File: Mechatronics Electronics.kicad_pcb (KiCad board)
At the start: 2 copper layers, 30.5 x 30 mm, 2 parts

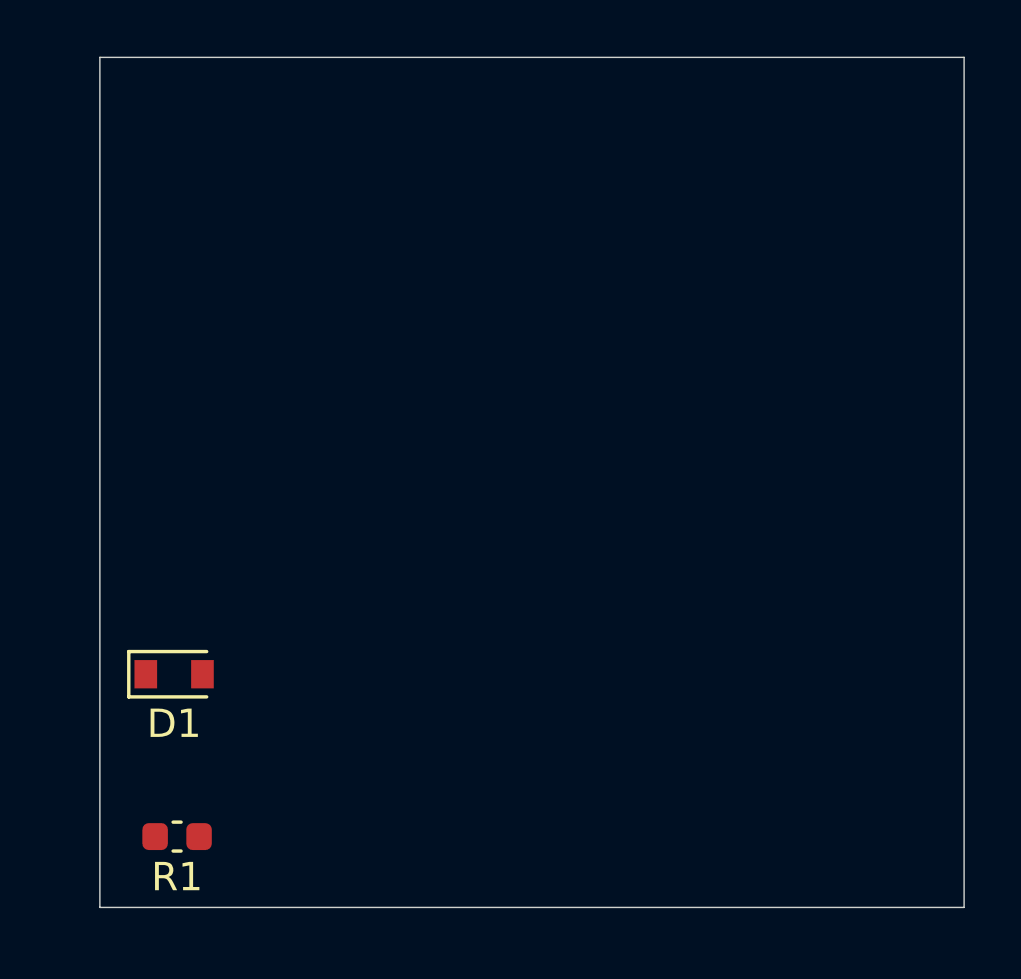
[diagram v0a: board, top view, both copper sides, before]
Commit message: Added TCAN4551-Q1 custom footprint/symbol and applied BGA microvia DRC rule
- Created and linked custom symbol + footprint for TCAN4551-Q1
- Added KiCad default MCIMX6D4AVT symbol
- Defined BGA_Area rule with microvia geometry:
  * Min annular width: 2 mil
  * Min via diameter: 8 mil
  * Min via hole size: 4 mil
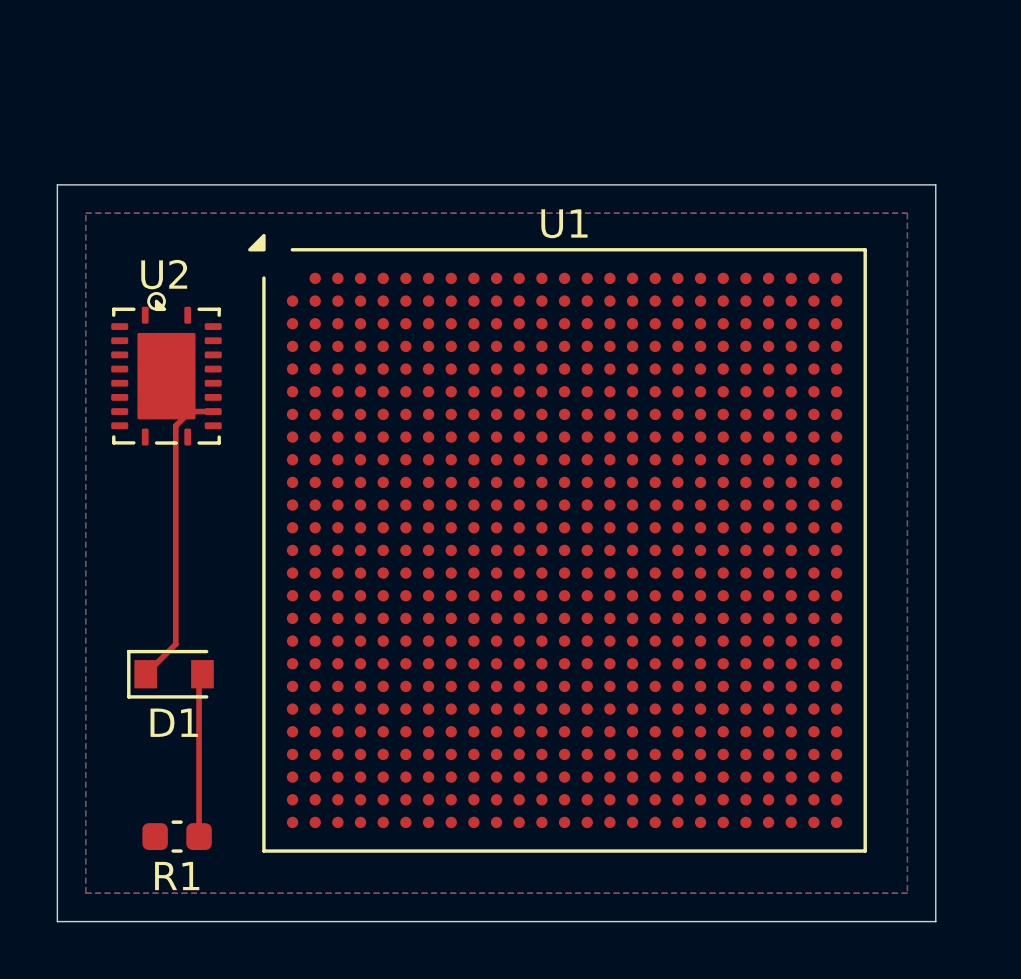
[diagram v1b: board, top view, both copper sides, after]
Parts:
- added U1: MCIMX6D4AVT, Package_BGA:BGA-624_21x21mm_Layout25x25_P0.8mm, F.Cu at (128.9, 93.4)
- added U2: TCAN4551-Q1, TCAN_Library:TCAN4551-Q1, F.Cu at (114.8, 87.3)
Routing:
- net GND: track 0.00 -> 10.7 mm
- net Net-(D1-A): track 0.00 -> 5.78 mm
- added copper zone on B.Cu, net GND
- added copper zone on F.Cu, net GND
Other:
- board size 30.5 x 30 mm -> 31 x 26 mm
